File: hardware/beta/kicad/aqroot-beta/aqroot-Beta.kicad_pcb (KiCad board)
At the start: 4 copper layers, 74 x 155 mm, 188 parts, among them J1 CH280QV10-CT_50P, J2 Molex_5025700893, J3 USB_C_Receptacle_USB2.0_16P, J4 JST-PH-2 BATTERY, J5 COMMUNITY_HEADER_2x13, J6 JST-PH-2 SPEAKER, Q1 AO3400A, SW1 BOOT, SW2 UP, SW3 DOWN, SW4 LEFT, SW5 RIGHT, SW6 A_SELECT, SW7 B_BACK, SW8 HOME, SW9 SW_SPDT, U1 ESP32-S3-WROOM-1, U10 USBLC6-2SC6, U11 BQ25185, U12 TPS63020, U13 TPS61023, U14 MAX17048, U15 TPS22918, U16 TCA9517ADGK, U17 TPS61169DCKR, U2 TCA9535PWR, U3 TCA9535PWR, U4 BMI270, U5 MAX98357A, U6 TSOP38238, U7 E07-400M10S, U8 E22-900M22S, U9 ST25R3916-AQET

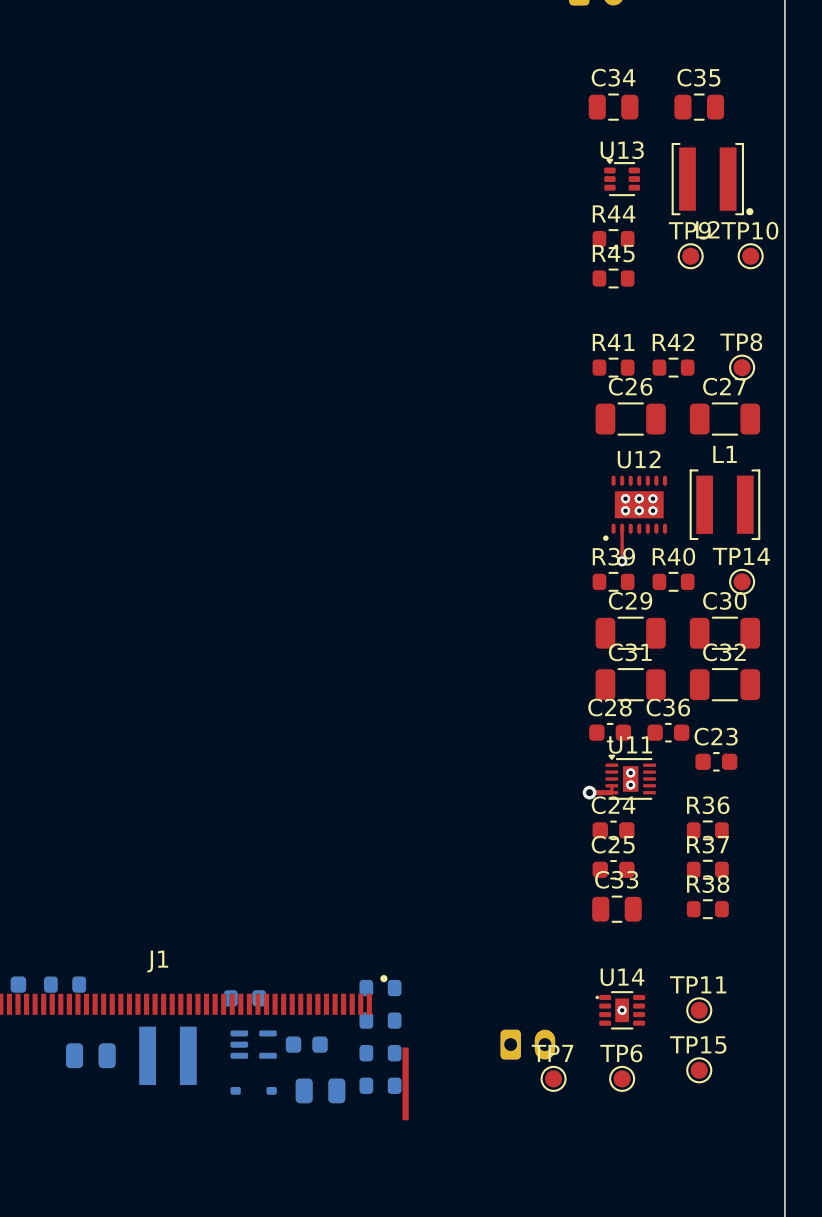
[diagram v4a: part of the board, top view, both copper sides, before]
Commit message: AQROOT Beta: route converters and BAT/SYS power rails
Routing Pass 1 resumed against the corrected width lock. All four
converter blocks and the BAT/SYS/+3V3 rails are routed and DRC-clean.
USB, E4, the E5 crossings, the +3V3 band crossing and the C55/U9 supply
are NOT routed, so Pass 1 still does not close.

83 tracks, 29 vias (16 THERMAL 0.25, 10 POWER 0.40, 3 SIGNAL 0.30).
15 nets carry copper: 9 fully routed - ILIM_VSET, R_FB_TOP, BL_SW,
LED_BOOST, BAT_PROTECTED_P, both L1 switch nodes, U11-TS_MR, U13-SW -
and 6 partial. Unconnected 499 -> 486.

Removed the pass-1A U12 pin-2 GND escape and its plane via: pin 2 now
ties directly to PGND_EP, which already carries 6 vias to In1. Shorter
return, and it cleared the board's only dangling via.

BAT_PROTECTED_P runs on B.Cu, 0.60 mm throughout, 36.24 mm, fully routed
to C25, C36, U14 and TP15. C24 (SYS), C25 (BAT) and C33 (SYS) interleave
in one column so the rails must cross; BAT may not use In2 (1.5 A at
0.5 oz needs 2.73 mm), so the crossing is taken between two outer
layers, which is the only arrangement keeping both rails at class width.
BQ25185_SYS runs on F.Cu at x=61.2, 81.04 mm, 0.50-0.80 mm rail with
0.20-0.25 mm escapes inside the authorised courtyards only.

Switch nodes kept minimal: U12 buck 2.70 mm / 1.35 mm2, U12 boost
6.89 mm / 3.44 mm2 (2.5x the buck because L1's pads face opposite pin
rows and the boost node must route around the inductor), U13 2.87 mm /
0.98 mm2, U17 4.55 mm / 2.27 mm2. C56 1 uF local CIN reaches U17 pin 5
in 1.62 mm, so the TI SNVSA40B 7.5.1 requirement is now met physically.

ISET deferred: U11 pin 8 is north of pin 7 but R37 is south of R36, so
the two programming nets must cross, and every via that takes the
crossing off-layer lands within 0.25 mm of the VBUS via, the VBUS escape
or the TS/MR run. U13's FB divider deferred as outside the section-6
scope.

C55 -> U9 is BLOCKED at class width by the same C50/C52 row that limited
C55's placement. NFC_5V_PA_PENDING needs 0.35 mm widt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
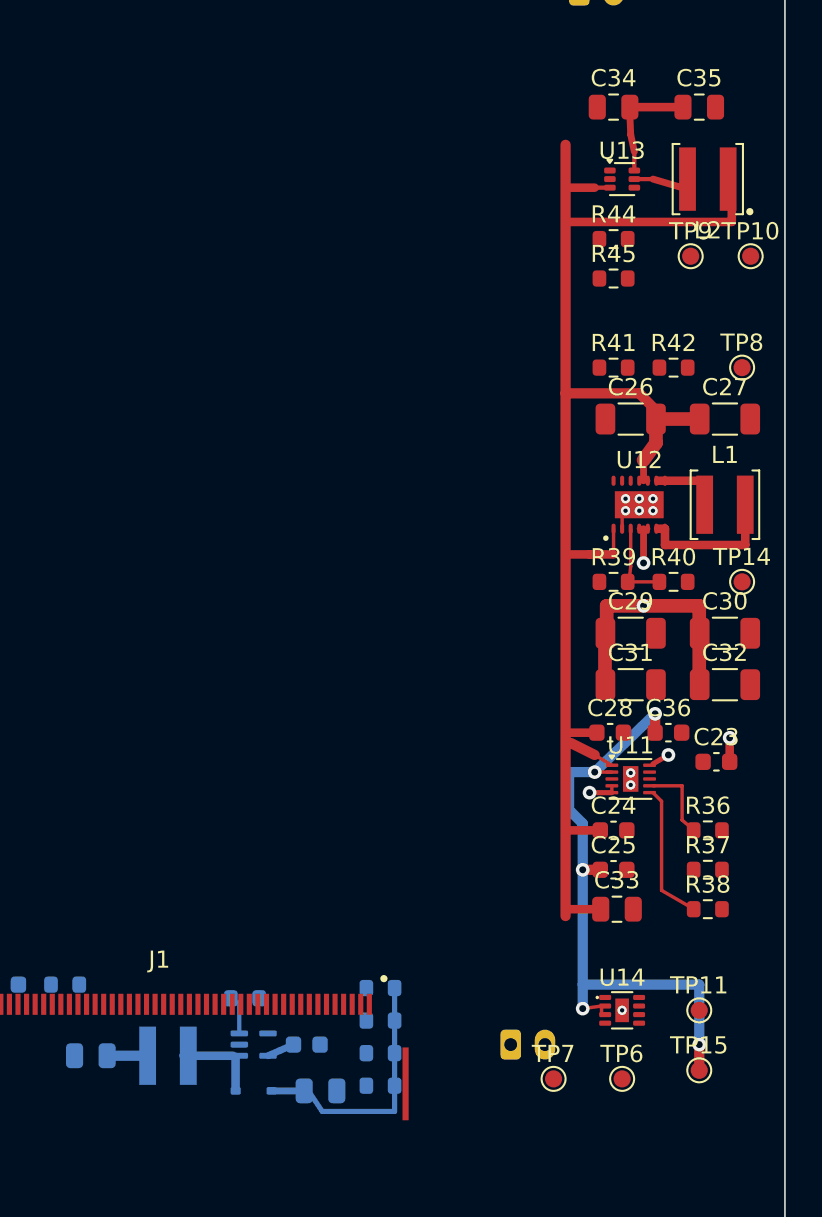
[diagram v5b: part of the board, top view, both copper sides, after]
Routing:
- net /01_POWER_TREE/BQ25185_SYS: track 0.00 -> 81.0 mm
- net /BAT_PROTECTED_P: track 0.00 -> 36.2 mm, vias 0 -> 5
- net +3V3: track 0.00 -> 21.0 mm, vias 0 -> 2
- net /03_SPI_A_DISPLAY_SD/LED_BOOST: track 0.00 -> 14.7 mm
- net Net-(U11-TS_MR): track 0.00 -> 8.10 mm
- net Net-(L1-Pad2): track 0.00 -> 6.89 mm
- net /01_POWER_TREE/USB_VBUS_CHG: track 0.00 -> 6.15 mm, vias 0 -> 2
- net /NFC_5V_PA_PENDING: track 0.00 -> 5.87 mm
- net /01_POWER_TREE/R_FB_TOP 1M: track 0.00 -> 4.91 mm
- net /01_POWER_TREE/ILIM_VSET: track 0.00 -> 4.62 mm
- net /03_SPI_A_DISPLAY_SD/BL_SW: track 0.00 -> 4.55 mm
- net Net-(U13-SW): track 0.00 -> 2.87 mm
- net Net-(L1-Pad1): track 0.00 -> 2.70 mm
- net /03_SPI_A_DISPLAY_SD/LED_K: track 0.00 -> 1.85 mm
- net GND: track 9.67 -> 8.97 mm, vias 21 -> 20

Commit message: AQROOT Beta: route C55 escape, ISET, E5 corridors and RF crossings
Routing Pass 1B. 0 DRC errors, placement unchanged, no new custom rule
added. USB is still not started, so Pass 1 does not close.

The authorised C55 width exception was NOT needed. The C50 pad2 to C52
pad1 gap is 0.950 mm, which takes the full 0.35 mm NFC_5V_PA width with
0.300 mm clearance each side - the capacitors were never the obstruction.
The real blocker was my own U9 pad-12 GND fanout via at (24.000, 25.560)
from the previous commit; pads 12 and 16 now share the (26.550, 25.560)
plane tie through a common rail south of U9, so the same three GND pins
stay tied and the lane opens. The only sub-width segments are the two
0.30 mm final approaches inside U9 courtyard, already covered by the
existing necking rule. C55 pad1 to U9 pin 10 is 5.92 mm routed (4.469
straight-line), pin 8 7.47 mm (4.875), all F.Cu, no via, 0.300 mm minimum
clearance. C19 untouched.

ISET now fully routed: 7.50 mm, 2 vias (0.25/0.50), pin 8 east then In2
beneath the ILIM run to R37, with TS/MR re-laid 0.2 mm west to clear the
via. U13 FB completed at 8.49 mm with 2 vias, taking its crossing of the
SYS escape on In2 under In1 GND; minimum SW-to-FB separation 1.59 mm on
different layers. BQ25185_SYS has 2 ratsnest items left, both to SW9,
whose EN partner is deferred - left as a pair.

E5 C-W: 280 mm over 5 nets (SD_CS_N, SPI_A x3, BTN_HOME_N) at 1.2 mm
pitch, In2, crossing both bands. E5 C-E: 320 mm over 10 nets (SPI_B x3,
SX1262 x5, CC1101 x2) at 1.0 mm pitch. +3V3 crossing 30 mm at 0.60 mm on
In2, 49.6 mohm, 11.6 mV at the derived 235 mA. E4 VBUS 34 mm at 0.50 mm
inside the east lane.

Rule mechanic worth recording: enclosedByArea can never be satisfied by a
track that enters or leaves a corridor, because the end cap always pokes
past the boundary. Corridor crossings therefore have to hand off by via
inside the corridor margin - which is what section 10 layer-transition
guidance asks for. All four crossing structures are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
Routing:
- net /SPI_A_SCK: track 0.00 -> 56.0 mm
- net /SPI_A_MOSI: track 0.00 -> 56.0 mm
- net /SPI_A_MISO: track 0.00 -> 56.0 mm
- net /SD_CS_N: track 0.00 -> 56.0 mm
- net /08_BUTTONS_EXPANDERS/BTN_HOME_N: track 0.00 -> 56.0 mm
- net +3V3: track 21.0 -> 76.0 mm, vias 2 -> 4
- net /01_POWER_TREE/USB_VBUS_CHG: track 6.15 -> 41.2 mm, vias 2 -> 5
- net /SX1262_RXEN: track 0.00 -> 32.0 mm
- net /SX1262_RST_N: track 0.00 -> 32.0 mm
- net /SX1262_DIO1: track 0.00 -> 32.0 mm
- net /SX1262_CS_N: track 0.00 -> 32.0 mm
- net /SX1262_BUSY: track 0.00 -> 32.0 mm
- net /SPI_B_SCK: track 0.00 -> 32.0 mm
- net /SPI_B_MOSI: track 0.00 -> 32.0 mm
- net /SPI_B_MISO: track 0.00 -> 32.0 mm
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
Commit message: AQROOT Beta: move C20 0.300 mm north to open the J3 USB escape
The authorised C20 move was +2 mm east. That is impossible, it was aimed
at the wrong constraint, and one figure I reported last pass was wrong.

Correction first: I reported the bypass corridors as west 1.325 mm (fits)
and east 0.925 mm (does not). The east corridor is also 1.325 mm - C20
pad2 right edge 36.450 to R31 pad1 left edge 37.775. The 0.900 mm I had
measured was the gap between C20 own two pads and I conflated the two.
Both corridors accommodate the 1.20 mm pair envelope, so widening one was
never the obstruction.

C20 verified from the netlist, not inferred: 4.7 uF 10 V X7R, 0805, pad1
USB_VBUS_RAW and pad2 GND - the USB VBUS bulk/bypass at the connector,
serving J3 pads A4/A9/B4/B9, U10 pin 5 (USBLC6 VBUS clamp) and R35 pin 1.

C20 is boxed in on all four sides by parts section 4 locks: west 0.730 mm
(R30), east 0.730 mm (R31), north 0.380 mm (U10), south 0.695 mm (J3). A
1.5-2.0 mm east move cannot be made without moving R31, which is
forbidden - and it would not have helped. J3 D+/D- pads run N P N P at
0.5 mm pitch, so separating the polarities needs exactly one layer hop,
and that hop needs a via row in the band between J3 pad row (147.070) and
C20 pad row (145.525): 0.20 clearance + 0.60 via pad + 0.20 + 0.30 track
+ 0.20 = 1.500 mm required against 1.545 mm available. It already fitted,
by 45 um, which is not a manufacturable margin. East and west moves do
not change that band at all and south shrinks it.

North is the only productive direction. C20 (35.000, 144.800) ->
(35.000, 144.500), 0.300 mm, keeping 0.080 mm courtyard clearance to U10
and taking the band to 1.845 mm - a 0.345 mm margin. That is 0.300 mm
rather than ~2 mm, honouring the "smallest move that provides a legal,
practical straight USB channel" instruction.

Its bypass role improves rather than degrades: pad1 to J3 A4 VBUS
3.193 -> 3.463 mm (+0.270), but pad1 to U10 pin 5 VBUS 4.734 -> 4.440
(-0.293) and pad2 to U10 pi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
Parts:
- moved C20 0.30 mm to (35.0, 144.5)
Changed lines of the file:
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@@
 	(footprint "Capacitor_SMD:C_0805_2012Metric"
 		(layer "F.Cu")
-		(at 35 144.8)
+		(at 35 144.5)
 		(descr "Capacitor SMD 0805 (2012 Metric), square (rectangular) end terminal, IPC-7351 nominal, (Body size source: IPC-SM-782 page 76, https://www.pcb-3d.com/wordpress/wp-content/uploads/ipc-sm-782a_amendment_1_and_2.pdf, https://docs.google.com/spreadsheets/d/1BsfQQcO9C6DZCsRaXUlFlo91Tg2WpOkGARC1WS5S8t0/edit?usp=sharing)")
 		(tags "capacitor")
@@
 	(footprint "C_0603_1608Metric"
 		(layer "B.Cu")
-		(at 28.5 79 180)
+		(at 46.1 82.5)
 		(descr "Capacitor SMD 0603 (1608 Metric), square (rectangular) end terminal, IPC-7351 nominal, (Body size source: IPC-SM-782 page 76, https://www.pcb-3d.com/wordpress/wp-content/uploads/ipc-sm-782a_amendment_1_and_2.pdf)")
 		(tags "capacitor")
-		(property "Reference" "C13"
-			(at 0 1.43 0)
+		(property "Reference" "C56"
+			(at 0 1.43 180)
 			(layer "B.SilkS")
 			(effects
@@
 			)
 		)
-		(property "Value" "100nF"
-			(at 0 -1.43 0)
+		(property "Value" "1uF"
+			(at 0 -1.43 180)
 			(layer "B.Fab")
 			(effects
@@
 		)
 		(property "Datasheet" ""
-			(at 0 0 0)
+			(at 0 0 180)
 			(layer "B.Fab")
 			(hide yes)
@@
 		)
 		(property "Description" ""
-			(at 0 0 0)
+			(at 0 0 180)
 			(layer "B.Fab")
 			(hide yes)
@@
 		)
 		(property "KiLib_Generator" "SMD_2terminal_chip_molded"
-			(at 0 0 0)
+			(at 0 0 180)
 			(layer "B.SilkS")
 			(hide yes)
@@
 		(duplicate_pad_numbers_are_jumpers no)
 		(fp_line
-			(start -0.14058 0.51)
-			(end 0.14058 0.51)
+			(start -0.14058 -0.51)
+			(end 0.14058 -0.51)
 			(stroke
 				(width 0.12)
@@
 		)
 		(fp_line
-			(start -0.14058 -0.51)
-			(end 0.14058 -0.51)
+			(start -0.14058 0.51)
+			(end 0.14058 0.51)
 			(stroke
 				(width 0.12)
@@
 		)
 		(fp_text user "${REFERENCE}"
-			(at 0 0 0)
+			(at 0 0 180)
 			(layer "B.Fab")
 			(effects
@@
 		)
 		(pad "1" smd roundrect
-			(at -0.775 0 180)
+			(at -0.775 0)
 			(size 0.9 0.95)
 			(layers "B.Cu" "B.Mask" "B.Paste")
@@
 		)
 		(pad "2" smd roundrect
-			(at 0.775 0 180)
+			(at 0.775 0)
 			(size 0.9 0.95)
 			(layers "B.Cu" "B.Mask" "B.Paste")
@@
 	(footprint "C_0603_1608Metric"
 		(layer "B.Cu")
-		(at 46.1 82.5)
+		(at 28.5 79 180)
 		(descr "Capacitor SMD 0603 (1608 Metric), square (rectangular) end terminal, IPC-7351 nominal, (Body size source: IPC-SM-782 page 76, https://www.pcb-3d.com/wordpress/wp-content/uploads/ipc-sm-782a_amendment_1_and_2.pdf)")
 		(tags "capacitor")
-		(property "Reference" "C56"
-			(at 0 1.43 180)
+		(property "Reference" "C13"
+			(at 0 1.43 0)
 			(layer "B.SilkS")
 			(effects
@@
 			)
 		)
-		(property "Value" "1uF"
-			(at 0 -1.43 180)
+		(property "Value" "100nF"
+			(at 0 -1.43 0)
 			(layer "B.Fab")
 			(effects
@@
 		)
 		(property "Datasheet" ""
-			(at 0 0 180)
+			(at 0 0 0)
 			(layer "B.Fab")
 			(hide yes)
@@
 		)
 		(property "Description" ""
-			(at 0 0 180)
+			(at 0 0 0)
 			(layer "B.Fab")
 			(hide yes)
@@
 		)
 		(property "KiLib_Generator" "SMD_2terminal_chip_molded"
-			(at 0 0 180)
+			(at 0 0 0)
 			(layer "B.SilkS")
 			(hide yes)
@@
 		(duplicate_pad_numbers_are_jumpers no)
 		(fp_line
-			(start -0.14058 -0.51)
-			(end 0.14058 -0.51)
+			(start -0.14058 0.51)
+			(end 0.14058 0.51)
 			(stroke
 				(width 0.12)
@@
 		)
 		(fp_line
-			(start -0.14058 0.51)
-			(end 0.14058 0.51)
+			(start -0.14058 -0.51)
+			(end 0.14058 -0.51)
 			(stroke
 				(width 0.12)
@@
 		)
 		(fp_text user "${REFERENCE}"
-			(at 0 0 180)
+			(at 0 0 0)
 			(layer "B.Fab")
 			(effects
@@
 		)
 		(pad "1" smd roundrect
-			(at -0.775 0)
+			(at -0.775 0 180)
 			(size 0.9 0.95)
 			(layers "B.Cu" "B.Mask" "B.Paste")
@@
 		)
 		(pad "2" smd roundrect
-			(at 0.775 0)
+			(at 0.775 0 180)
 			(size 0.9 0.95)
 			(layers "B.Cu" "B.Mask" "B.Paste")

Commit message: USB: route J3->U10->R33/R34->U1 at approved 0.25/0.20 geometry
Closes the Routing Pass 1 USB blocker. 0 DRC errors.

The four earlier passes failed because 0.30 mm put the track width at the exact
maximum the connector's 0.5 mm pad pitch permits, leaving 0.000 mm of margin on
every escape.  At fixed pitch the adjacent-copper gap is 0.5 - W and depends on
W alone, while Zdiff depends on W and S, so the two trade independently:
0.25/0.20 gives 97.6 ohm (+8.4%, inside the USB 2.0 +/-15% window) and 0.250 mm
of gap.  0.25/0.14 would hit 90.2 ohm but needs a P-to-N clearance exception;
8 ohm was traded to avoid weakening any clearance rule.

Rules: USB track_width -> min 0.23 / opt 0.25 / max 0.27; diff_pair_uncoupled
max 17 mm added; USB_D netclass to 0.25/0.20 with a 0.25/0.55 via class.
diff_pair_gap retained at 0.18/0.20/0.24.  No clearance rule changed, no
exception added, no broad exclusion.

Two mechanics: a 0.55 mm via pad on a 0.45 mm pair pitch clashes with the other
polarity's track whichever side transitions first - and no manufacturable
through-via is small enough - so both polarities splay symmetrically at every
transition.  And the on-pitch diff_pair_gap comes out at 0.250 mm, 0.010 over
the max, which the approved width tolerance fixes: on-pitch segments carry
0.26 mm for a gap of exactly 0.240 mm.

A7 (N) is the single polarity that hops, on B.Cu at y=146.200, which vacates the
x=35.25 lane so A6 and B6 (both P) merge over the top of it - one crossing
resolving both merges is the only arrangement that fits the 1.845 mm band.

J3->U1: P 81.14 mm, N 89.41 mm, skew 8.27 mm (~60 ps, 0.07% of a Full Speed bit;
architectural, R33 sits west of U10 and R34 east).  6 USB vias, max local
uncoupled 13.35 mm of the 17 mm budget.  E4 on In2 only, transition vias at
y=116.000 and y=86.000 - all outside Y88-114 - min USB<->VBUS 1.475 mm.

E4 In2 reads ~139.8 ohm vs the 90 ohm target over ~216 ps; accepted by analysis
for Full Speed and recorded as USB E4 IMPEDANCE DISC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
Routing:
- net /USB_D_MCU_N: track 0.00 -> 75.4 mm, vias 0 -> 2
- net /USB_D_MCU_P: track 0.00 -> 67.0 mm, vias 0 -> 2
- net /01_POWER_TREE/USB_D_CONN_P: track 0.00 -> 11.0 mm
- net /01_POWER_TREE/USB_D_CONN_N: track 0.00 -> 9.32 mm, vias 0 -> 2
- net /01_POWER_TREE/USB_D_ESD_N: track 0.00 -> 4.73 mm
- net /01_POWER_TREE/USB_D_ESD_P: track 0.00 -> 3.08 mm
